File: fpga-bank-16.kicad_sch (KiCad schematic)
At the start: 1 part, among them U1 XC7K410T-2FFG900I

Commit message: Updated schematic page fields
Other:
- company: (none) -> Antmicro Ltd.
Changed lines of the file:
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@@
   (title_block
     (title "K410T devboard")
-    (date "2023-01-04")
+    (date "2023-01-27")
     (rev "0.0.99")
+    (company "Antmicro Ltd.")
   )
   (no_connect (at 143.51 109.22))

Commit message: Adding JTAG to FMC connector - in progress
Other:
- company: Antmicro Ltd. -> (none)
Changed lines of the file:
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@@
   (title_block
     (title "K410T devboard")
-    (date "2023-01-27")
+    (date "2023-01-04")
     (rev "0.0.99")
-    (company "Antmicro Ltd.")
   )
   (no_connect (at 143.51 109.22))

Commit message: Bump revision to 1.0.0. Update name on schematic and PCB sheets
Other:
- title: K410T devboard -> Kintex 410T devboard

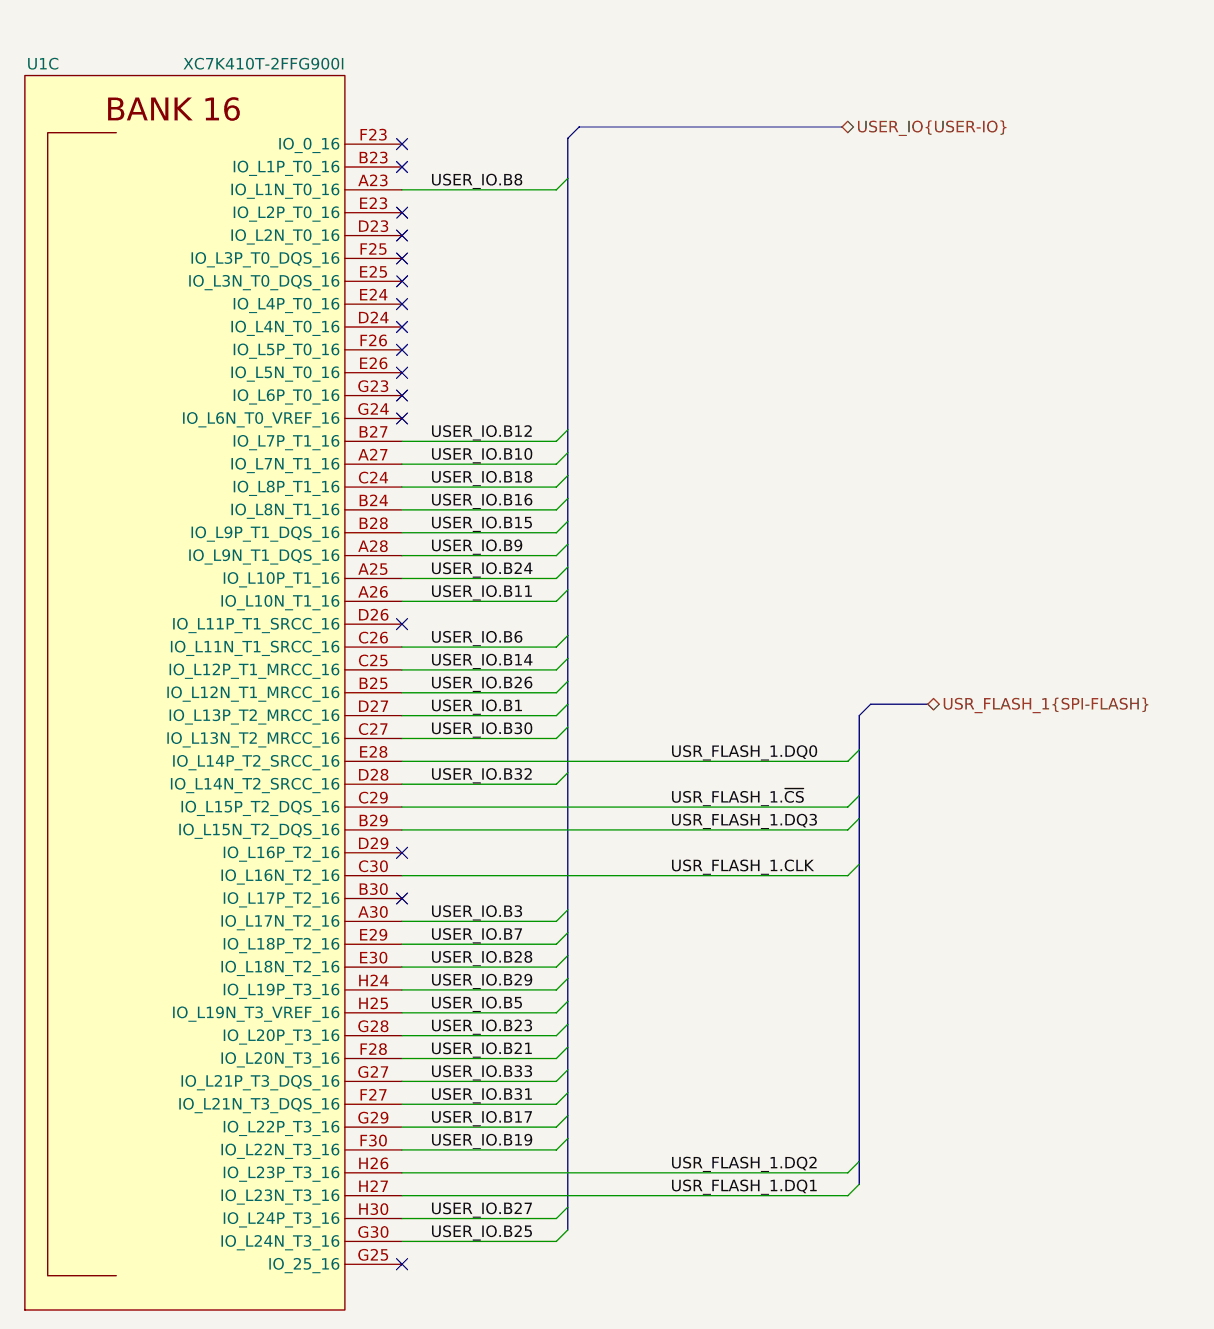
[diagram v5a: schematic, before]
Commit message: Introduce component standardization
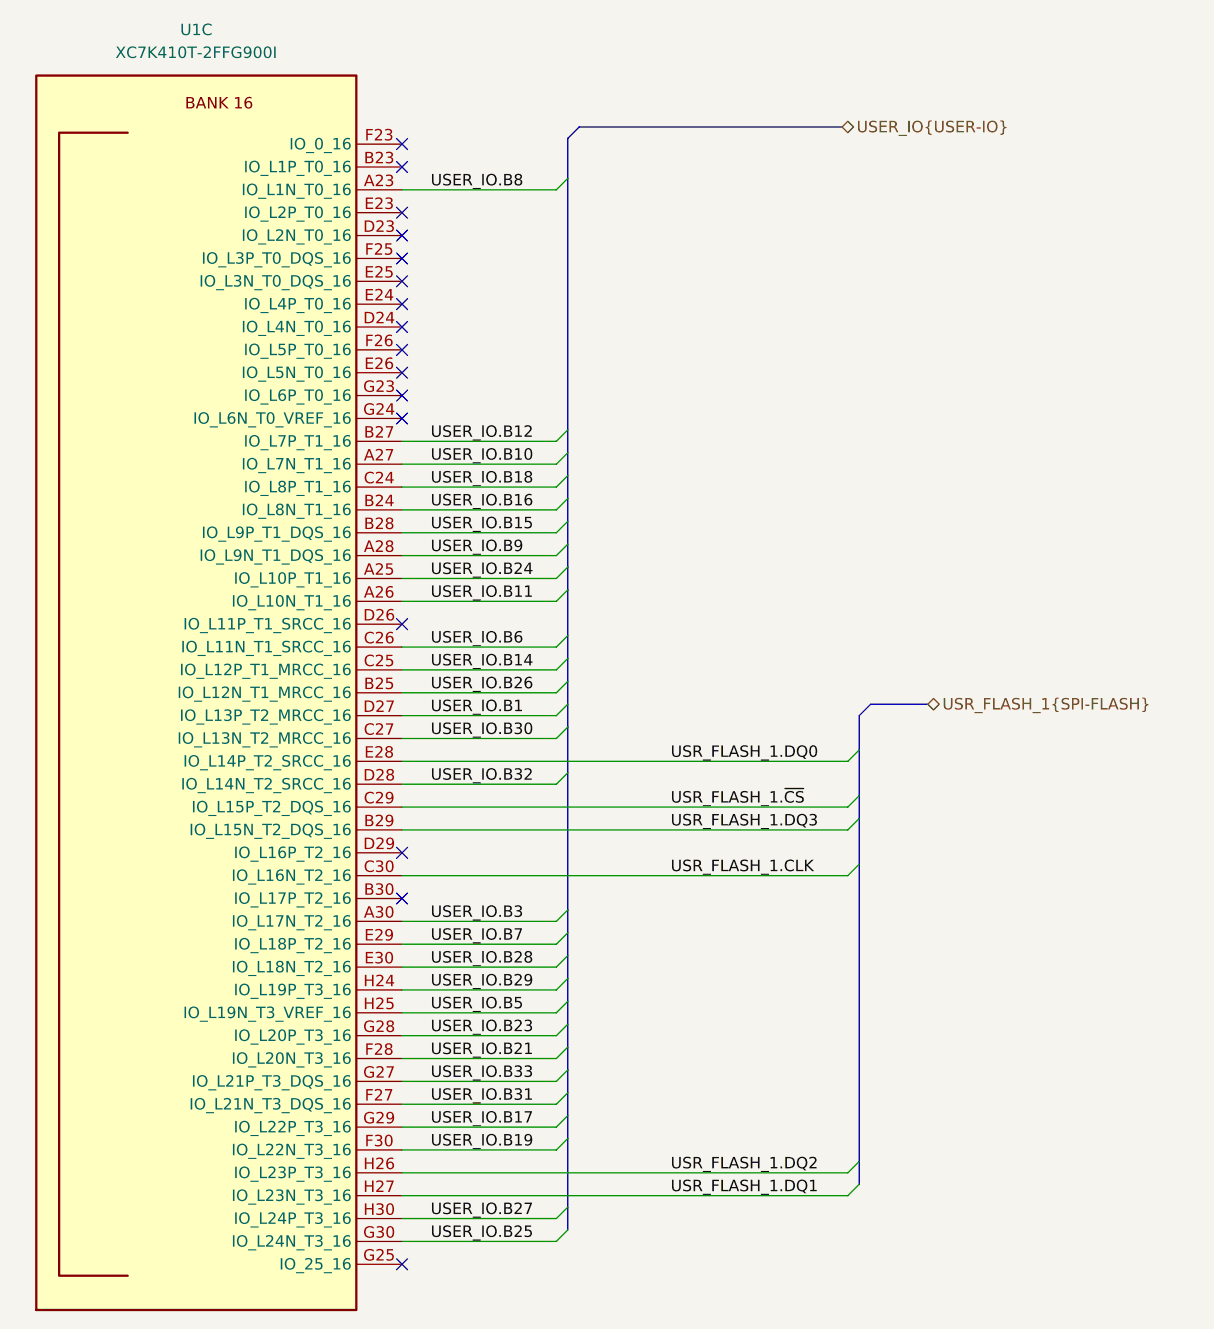
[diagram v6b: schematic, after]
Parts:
- U1: Author (none) -> Antmicro; License (none) -> Apache-2.0
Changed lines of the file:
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@@
     (title "Kintex 410T devboard")
     (date "2023-02-01")
-    (rev "1.0.0")
+    (rev "1.1.1")
   )
   (no_connect (at 143.51 109.22))
@@
     (effects (font (size 1.27 1.27)) (justify left))
   )
-  (symbol (lib_id "K410T-devboard:XC7K410T-2FFG900I") (at 119.38 144.78 0) (unit 3)
-    (in_bom yes) (on_board yes)
-    (property "Reference" "U1" (id 0) (at 105.41 74.93 0)
-      (effects (font (size 1.27 1.27)) (justify right))
+  (symbol (lib_id "K410T-devboard:XC7K410T-2FFG900I") (at 143.51 83.82 0) (unit 3)
+    (in_bom yes) (on_board yes) (fields_autoplaced)
+    (property "Reference" "U1" (id 0) (at 120.65 71.12 0)
+      (effects (font (size 1.27 1.27) (thickness 0.15)))
     )
-    (property "Value" "XC7K410T-2FFG900I" (id 1) (at 137.16 74.93 0)
-      (effects (font (size 1.27 1.27)) (justify right))
+    (property "Value" "XC7K410T-2FFG900I" (id 1) (at 120.65 73.66 0)
+      (effects (font (size 1.27 1.27) (thickness 0.15)))
     )
-    (property "Footprint" "K410T-devboard-footprints:xc7k410t-2ffg900I" (id 2) (at 119.38 219.71 0)
-      (effects (font (size 1.27 1.27)) hide)
+    (property "Footprint" "K410T-devboard-footprints:xc7k410t-2ffg900I" (id 2) (at 143.51 57.15 0)
+      (effects (font (size 1.27 1.27) (thickness 0.15)) (justify left bottom) hide)
     )
-    (property "Datasheet" "https://eu.mouser.com/datasheet/2/903/ds180_7Series_Overview-1591537.pdf" (id 3) (at 119.38 222.25 0)
-      (effects (font (size 1.27 1.27)) hide)
+    (property "Datasheet" "https://eu.mouser.com/datasheet/2/903/ds180_7Series_Overview-1591537.pdf" (id 3) (at 143.51 59.69 0)
+      (effects (font (size 1.27 1.27) (thickness 0.15)) (justify left bottom) hide)
     )
-    (property "Manufacturer" "Xilinx" (id 4) (at 119.38 214.63 0)
-      (effects (font (size 1.27 1.27)) hide)
+    (property "Manufacturer" "Xilinx" (id 4) (at 143.51 62.23 0)
+      (effects (font (size 1.27 1.27) (thickness 0.15)) (justify left bottom) hide)
     )
-    (property "MPN" "XC7K410T-2FFG900I" (id 5) (at 119.38 217.17 0)
-      (effects (font (size 1.27 1.27)) hide)
+    (property "MPN" "XC7K410T-2FFG900I" (id 5) (at 143.51 64.77 0)
+      (effects (font (size 1.27 1.27) (thickness 0.15)) (justify left bottom) hide)
+    )
+    (property "Author" "Antmicro" (id 6) (at 143.51 67.31 0)
+      (effects (font (size 1.27 1.27) (thickness 0.15)) (justify left bottom) hide)
+    )
+    (property "License" "Apache-2.0" (id 7) (at 143.51 69.85 0)
+      (effects (font (size 1.27 1.27) (thickness 0.15)) (justify left bottom) hide)
     )
     (pin "AA20")
@@
     (pin "Y12")
     (pin "Y22")
-    (pin "C10")
-    (pin "M11")
-    (pin "M13")
-    (pin "M15")
-    (pin "M17")
-    (pin "N10")
-    (pin "N12")
-    (pin "N14")
-    (pin "N16")
-    (pin "N18")
-    (pin "P11")
-    (pin "P13")
-    (pin "P14")
-    (pin "P15")
-    (pin "P17")
-    (pin "R10")
-    (pin "R12")
-    (pin "R16")
-    (pin "R18")
-    (pin "T11")
-    (pin "T13")
-    (pin "T17")
-    (pin "U10")
-    (pin "U12")
-    (pin "U16")
-    (pin "U18")
-    (pin "V11")
-    (pin "V13")
-    (pin "V15")
-    (pin "V17")
-    (pin "W10")
-    (pin "W12")
-    (pin "W14")
-    (pin "W16")
-    (pin "W18")
     (pin "A1")
     (pin "A14")
@@
     (pin "B9")
     (pin "C1")
+    (pin "C10")
     (pin "C18")
     (pin "C2")
@@
     (pin "L6")
     (pin "L9")
+    (pin "M11")
     (pin "M12")
+    (pin "M13")
     (pin "M14")
+    (pin "M15")
     (pin "M16")
+    (pin "M17")
     (pin "M18")
     (pin "M21")
@@
     (pin "M9")
     (pin "N1")
+    (pin "N10")
     (pin "N11")
+    (pin "N12")
     (pin "N13")
+    (pin "N14")
     (pin "N15")
+    (pin "N16")
     (pin "N17")
+    (pin "N18")
     (pin "N2")
     (pin "N28")
@@
     (pin "N9")
     (pin "P10")
+    (pin "P11")
     (pin "P12")
+    (pin "P13")
+    (pin "P14")
+    (pin "P15")
     (pin "P16")
+    (pin "P17")
     (pin "P18")
     (pin "P25")
@@
     (pin "P9")
     (pin "R1")
+    (pin "R10")
     (pin "R11")
+    (pin "R12")
     (pin "R13")
+    (pin "R16")
     (pin "R17")
+    (pin "R18")
     (pin "R2")
     (pin "R22")
@@
     (pin "R9")
     (pin "T10")
+    (pin "T11")
     (pin "T12")
+    (pin "T13")
     (pin "T16")
+    (pin "T17")
     (pin "T18")
     (pin "T19")
@@
     (pin "T8")
     (pin "U1")
+    (pin "U10")
     (pin "U11")
+    (pin "U12")
     (pin "U13")
+    (pin "U16")
     (pin "U17")
+    (pin "U18")
     (pin "U2")
     (pin "U26")
@@
     (pin "U9")
     (pin "V10")
+    (pin "V11")
     (pin "V12")
+    (pin "V13")
     (pin "V14")
+    (pin "V15")
     (pin "V16")
+    (pin "V17")
     (pin "V18")
     (pin "V23")
@@
     (pin "V9")
     (pin "W1")
+    (pin "W10")
     (pin "W11")
+    (pin "W12")
     (pin "W13")
+    (pin "W14")
     (pin "W15")
+    (pin "W16")
     (pin "W17")
+    (pin "W18")
     (pin "W2")
     (pin "W20")
